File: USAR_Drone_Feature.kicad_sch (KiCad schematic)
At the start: 64 parts, among them J1 DB128L-5.08-2P-BK-S, J10 Conn_01x04_Socket, J3 Conn_01x04_Socket, J4 Conn_01x04_Socket, J5 Conn_01x04_Socket, J6 Conn_01x04_Socket, J7 Conn_02x04_Odd_Even, J8 Conn_01x04_Socket, SW1 TS-1088-AR02016, SW2 TS-1088-AR02016, U1 AMS1117-3.3, U2 TSR 1-2450_C6886877, U3 AMS1117-3.3, U4 ESP32-S3-WROOM-1(N16R8)

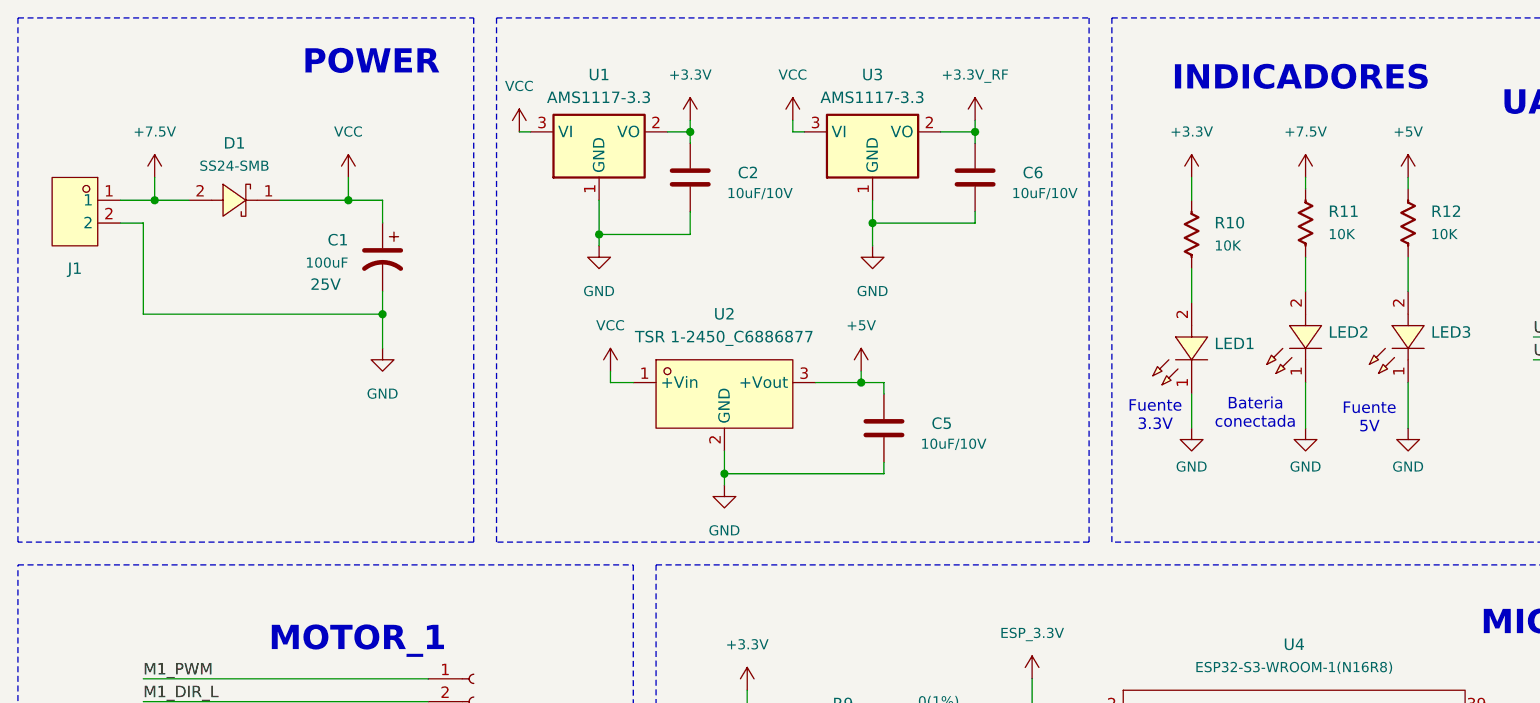
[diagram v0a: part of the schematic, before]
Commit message: Add Buck Converter Fixed 5V
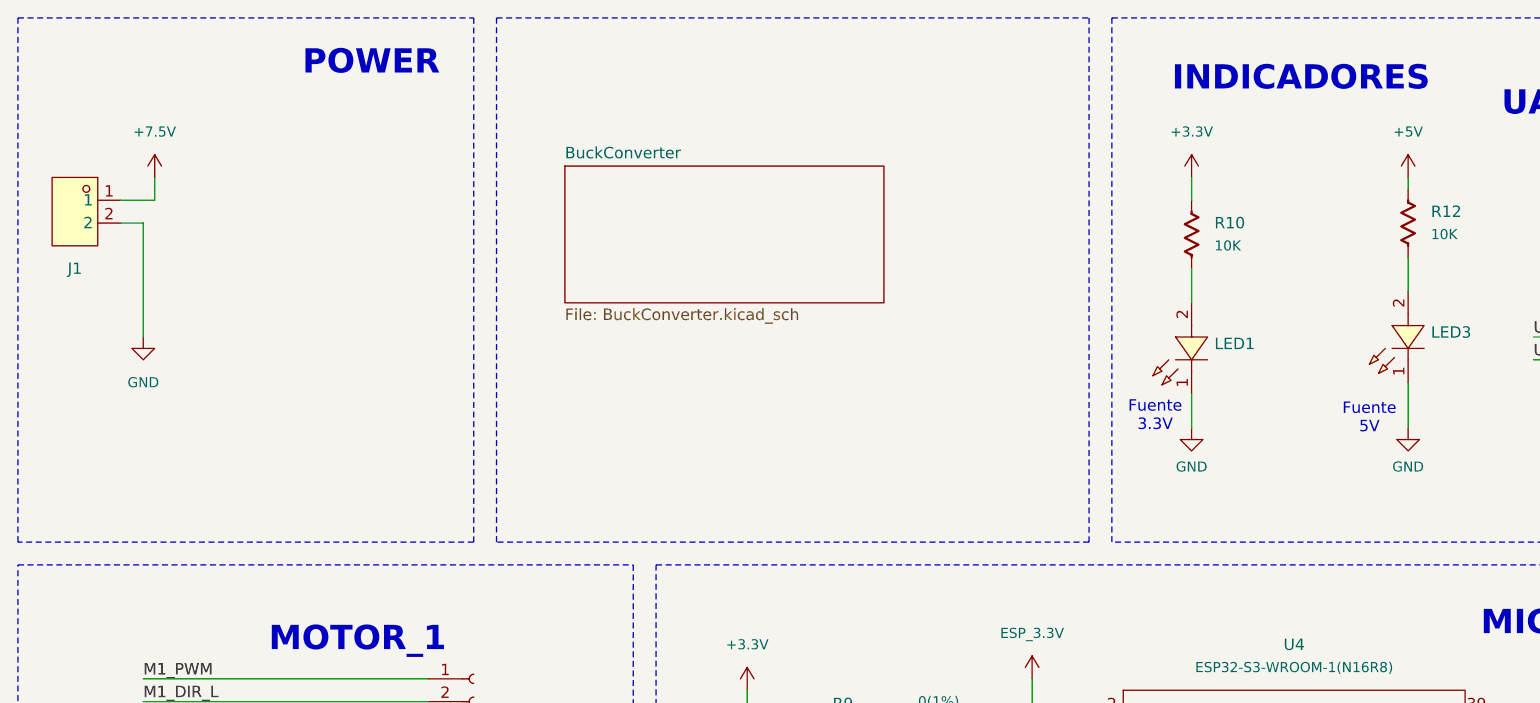
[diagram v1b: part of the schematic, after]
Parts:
- removed C1: 100uF, PCM_Capacitor_THT_US_AKL:CP_Radial_D4.0mm_P2.00mm, symbol PCM_Capacitor_US_AKL:CP_Radial_D4.0mm_P2.00mm
- removed C2, C5, C6: 10uF/10V, PCM_Capacitor_SMD_AKL:C_0805_2012Metric, symbol PCM_Capacitor_US_AKL:C_0805
- removed D1: SS24-SMB, EasyEDA:SMB_L4.3-W3.6-LS5.3-RD, symbol EasyEDA:SS24-SMB
- removed LED2: XL-1608SURC-06, EasyEDA:LED0603-RD_RED, symbol EasyEDA:XL-1608SURC-06
- removed R11: 10K, PCM_Resistor_SMD_AKL:R_0603_1608Metric, symbol PCM_Resistor_US_AKL:R_0603
- removed U1, U3: AMS1117-3.3, Package_TO_SOT_SMD:SOT-223-3_TabPin2, symbol Regulator_Linear:AMS1117-3.3
- removed U2: TSR 1-2450_C6886877, EasyEDA:PWRM-TH_L11.7-W7.5_TSR1-2450, symbol EasyEDA:TSR1-2450_C6886877
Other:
- added sheet BuckConverter (BuckConverter.kicad_sch)
- note removed: "Bateria conectada"

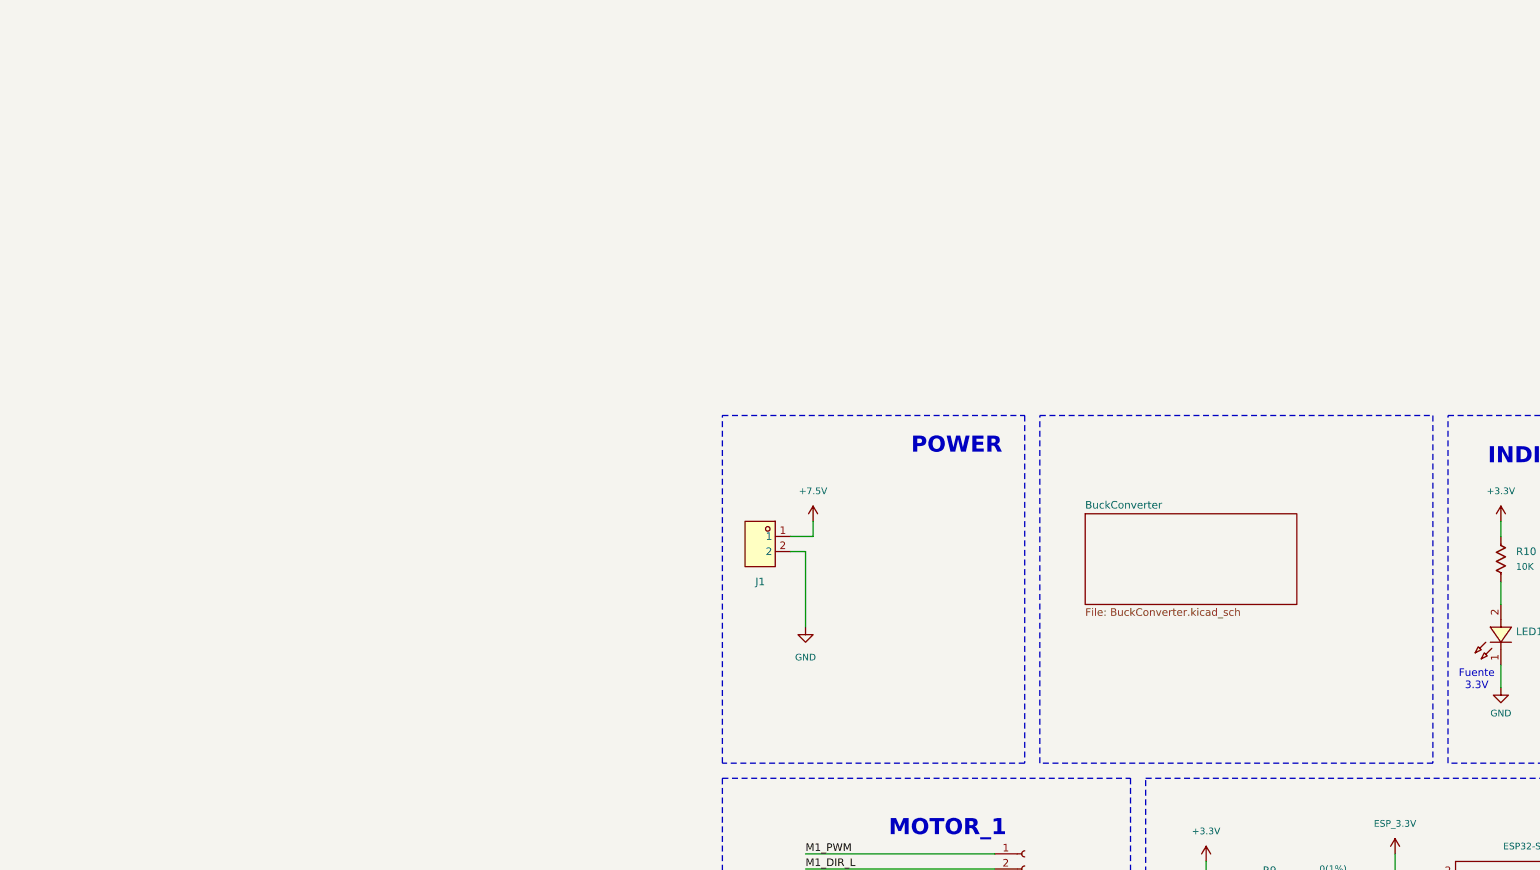
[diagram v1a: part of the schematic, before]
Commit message: etiquetar cables
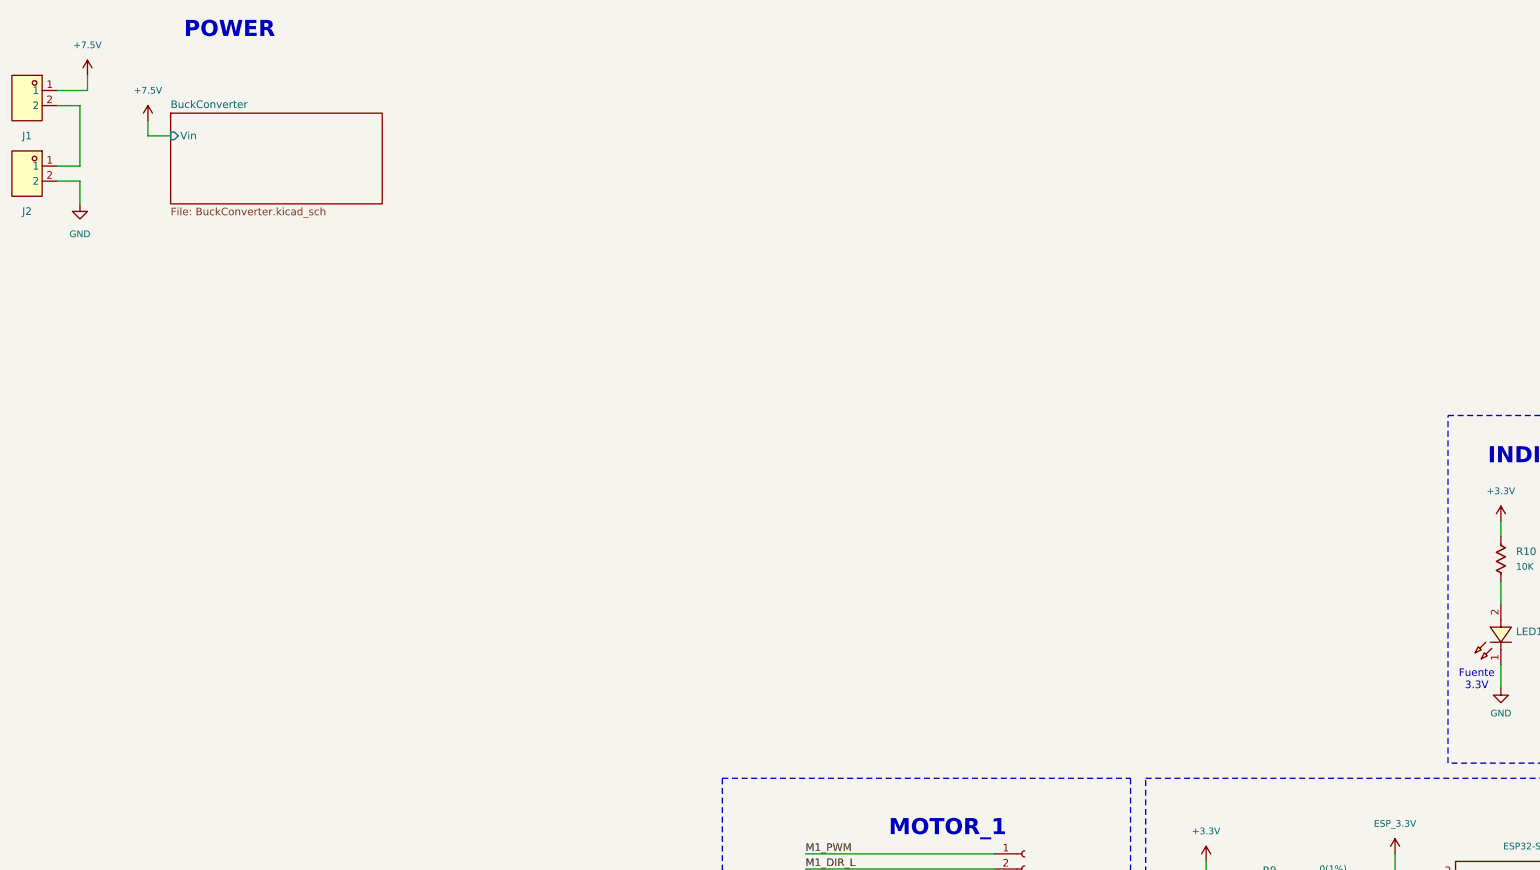
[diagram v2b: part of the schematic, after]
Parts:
- added J2: DB128L-5.08-2P-BK-S, EasyEDA:CONN-TH_2P-P5.08_DB128L-5.08-2P-BK-S, symbol EasyEDA:DB128L-5.08-2P-BK-S
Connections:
- net GND: now also J2.2; no longer J1.2
- new net: J1.2, J2.1
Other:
- sheet BuckConverter ports: added Vin; removed none
- moved on the sheet: J1

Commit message: add LDO 3v3, change buckconverter sheet to Power Rails
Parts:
- removed C11: 0.1uF/10V, PCM_Capacitor_SMD_AKL:C_0603_1608Metric, symbol PCM_Capacitor_US_AKL:C_0603
- removed C14: 1uF, PCM_Capacitor_SMD_AKL:C_0805_2012Metric, symbol PCM_Capacitor_US_AKL:C_0805
- removed R23, R24: 10K, PCM_Resistor_SMD_AKL:R_0603_1608Metric, symbol PCM_Resistor_US_AKL:R_0603
- C10: value 1uF/10V -> 1uF 25V
- C8: value 0.1uF/10V -> 100nF 25V
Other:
- sheet BuckConverter renamed POWER RAILS
- sheet POWER RAILS: file BuckConverter.kicad_sch -> PowerRails
- moved on the sheet: C10, C12, C13, C3, C4, C7, C8, C9, D2, D3, D4, H1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

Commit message: modificacion general de esquematico
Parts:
- removed C13: 1uF/10V, PCM_Capacitor_SMD_AKL:C_0805_2012Metric, symbol PCM_Capacitor_US_AKL:C_0805
- added D5, D6: ESD5Z3.3T, PCM_Diode_SMD_AKL:D_SOD-523, symbol PCM_Diode_TVS_AKL:ESD5Z3.3T
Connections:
- net +3.3V_RF is gone; now on net +3V3: J7.2 (Pin_2), R26.1
- net BOOT: now also D5.1 (K)
- net GND: now also D5.2 (A), D6.2 (A)
- net RST: now also D6.1 (K)
- net +3.3V renamed +3V3
- net ESP_3.3V: no longer names the net of R9.2, U4.2 (3V3)
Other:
- removed sheet POWER RAILS
- added sheet PowerRails (BuckConverter.kicad_sch)
- moved on the sheet: C10, C12, C3, C4, C7, C8, C9, D2, D3, D4, H1, H2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

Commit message: asignacion de huellas, valores y lcsc part #, dejar de rastrear .history/
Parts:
- removed J10, J3, J8: Conn_01x04_Socket, EasyEDA:CONN-TH_B4B-PH-K-S, symbol Connector:Conn_01x04_Socket
- removed R30, R31: 10K, PCM_Resistor_SMD_AKL:R_0603_1608Metric, symbol PCM_Resistor_US_AKL:R_0603
- added JP1, JP2: SolderJumper_2_Open, PCM_SparkFun-Jumper:Jumper_2_NO, symbol Jumper:SolderJumper_2_Open
- C1: renamed from C7; LCSC Part (none) -> C326595
- C2: renamed from C8; LCSC Part (none) -> C14663
- C3: renamed from C10; LCSC Part (none) -> 5370002
- C4: renamed from C3; value 1uF/10V -> 1uF 25V; LCSC Part (none) -> 5370002
- C5: renamed from C4; value 0.1uF/10V -> 100nF 25V; LCSC Part (none) -> C14663
- C6: renamed from C9; value 0.1uF/10V -> 100nF 25V; LCSC Part (none) -> C14663
- C7: renamed from C12; value 0.1uF/10V -> 100nF 25V; LCSC Part (none) -> C14663
- D2: renamed from D3; LCSC Part (none) -> C2936975
- D3: renamed from D4; LCSC Part (none) -> C2936975
- D4: renamed from D5; LCSC Part (none) -> C61148
- D5: renamed from D6; LCSC Part (none) -> C61148
- J3: renamed from J7; now left out of the parts list
- J4: renamed from J6; LCSC Part (none) -> C144395
- J5: LCSC Part (none) -> C144395
- J6: renamed from J4; LCSC Part (none) -> C144395
- R1: renamed from R15; LCSC Part (none) -> C125891
- R10: renamed from R26; LCSC Part (none) -> C860067
- R11: renamed from R27; LCSC Part (none) -> C860067
- R12: renamed from R9; LCSC Part (none) -> C100044
- R13, R14: LCSC Part (none) -> C113303
- R15: renamed from R28; LCSC Part (none) -> C113303
- R16: renamed from R29; LCSC Part (none) -> C113303
- R17: renamed from R19; LCSC Part (none) -> C860067
- R18: renamed from R22; LCSC Part (none) -> C860067
- R19: renamed from R5; LCSC Part (none) -> C860067
- R2: renamed from R16; LCSC Part (none) -> C125891
- R3: renamed from R17; LCSC Part (none) -> C108407
- R4: renamed from R18; LCSC Part (none) -> C108407
- R5: renamed from R20; LCSC Part (none) -> C860067
- R6: renamed from R21; LCSC Part (none) -> C860067
- R7: renamed from R10; LCSC Part (none) -> C860067
- R8: renamed from R12; LCSC Part (none) -> C860067
- R9: renamed from R25; LCSC Part (none) -> C860067
- renumbered D2 to D1, H4 to H1, H3 to H2, H2 to H3, H1 to H4, LED3 to LED2, U4 to U1
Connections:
- net +3V3: now also J5.4 (Pin_4), JP2.2 (B)
- net +5V: now also JP1.1 (A); no longer J4.1 (Pin_1)
- net GND: now also J5.3 (Pin_3)
- net I2C_SCL: now also J5.2 (Pin_2); no longer J5.3 (Pin_3), J5.4 (Pin_4)
- net I2C_SDA: no longer J5.2 (Pin_2)
- new net: J4.1 (Pin_1), JP1.2 (B), JP2.1 (A)
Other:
- note removed: "MOTOR_1"
- note removed: "SPI_AUX"
- moved on the sheet: J4

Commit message: pcb desing done, add productions files
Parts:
- removed R12: 0(1%), PCM_Resistor_SMD_AKL:R_0603_1608Metric, symbol PCM_Resistor_US_AKL:R_0603
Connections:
- net +3V3: now also U1.2 (3V3)
- net +5V: now also D1.2
- net +7.5V: now also R5.1
- net DN: now reaches R3.1, USB1.5 (DN2), USB1.7 (DN1)
- net DP: now reaches R4.1, USB1.6 (DP1), USB1.8 (DP2)
- net BATTERY1_LEVEL: no longer names the net of U1.8 (IO15)
- net CE_AUX: no longer names the net of U1.12 (IO8)
- net CS_AUX: no longer names the net of U1.6 (IO6)
- net FL_PWR_DRIVERS: no longer names the net of U1.11 (IO18)
- net I2C_SCL renamed I2C_N
- net I2C_N: now also R16.2
- net I2C_SDA renamed I2C_P
- net I2C_P: no longer R16.2
- net M1_DIR_L: no longer names the net of U1.20 (IO12)
- net M1_DIR_R: no longer names the net of U1.19 (IO11)
- net M1_PWM: no longer names the net of U1.9 (IO16)
- net M2_PWM: no longer names the net of U1.10 (IO17)
- net UART_RX0 renamed UART_P
- net UART_P: now also U1.37 (TXD0); no longer U1.36 (RXD0)
- net UART_TX0 renamed UART_N
- net UART_N: now also U1.36 (RXD0); no longer U1.37 (TXD0)
- removed net VCC: D1.2, R5.1
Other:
- note added: "3V-5V"
- note added: "Battery"
- note added: "Cámara Térmica MLX90640"
- note added: "MG90S"
- note added: "Modulo Radar Novelda X4M200"
- note added: "RX"
- note added: "SCL"
- note added: "SDA"
- note added: "TX"
- note added: "switch ON/OFF"
- moved on the sheet: J6, R19

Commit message: ajuste de agujeros
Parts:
- J3: now not fitted
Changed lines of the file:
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@@
 		(on_board yes)
 		(in_pos_files yes)
-		(dnp no)
+		(dnp yes)
 		(property "Reference" "J3"
 			(at 191.77 226.0599 90)
